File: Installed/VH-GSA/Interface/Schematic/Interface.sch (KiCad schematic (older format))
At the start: 32 parts, among them J1 RJ45, J2 RJ12, J3 RJ12, P1 USB_B, P10 USB_A, P11 USB_A, P12 USB_A, P13 USB_A, P14 USB_A, P15 USB_A, P16 USB_A, P17 USB_A, P2 USB_B, P3 CONN_01X02, P4 USB_B, P5 USB_B, P6 CONN_01X06, P7 CONN_01X06, P8 CONN_01X06, P9 CONN_01X06, SW1 SW_DPDT_x2, U1 MAX232

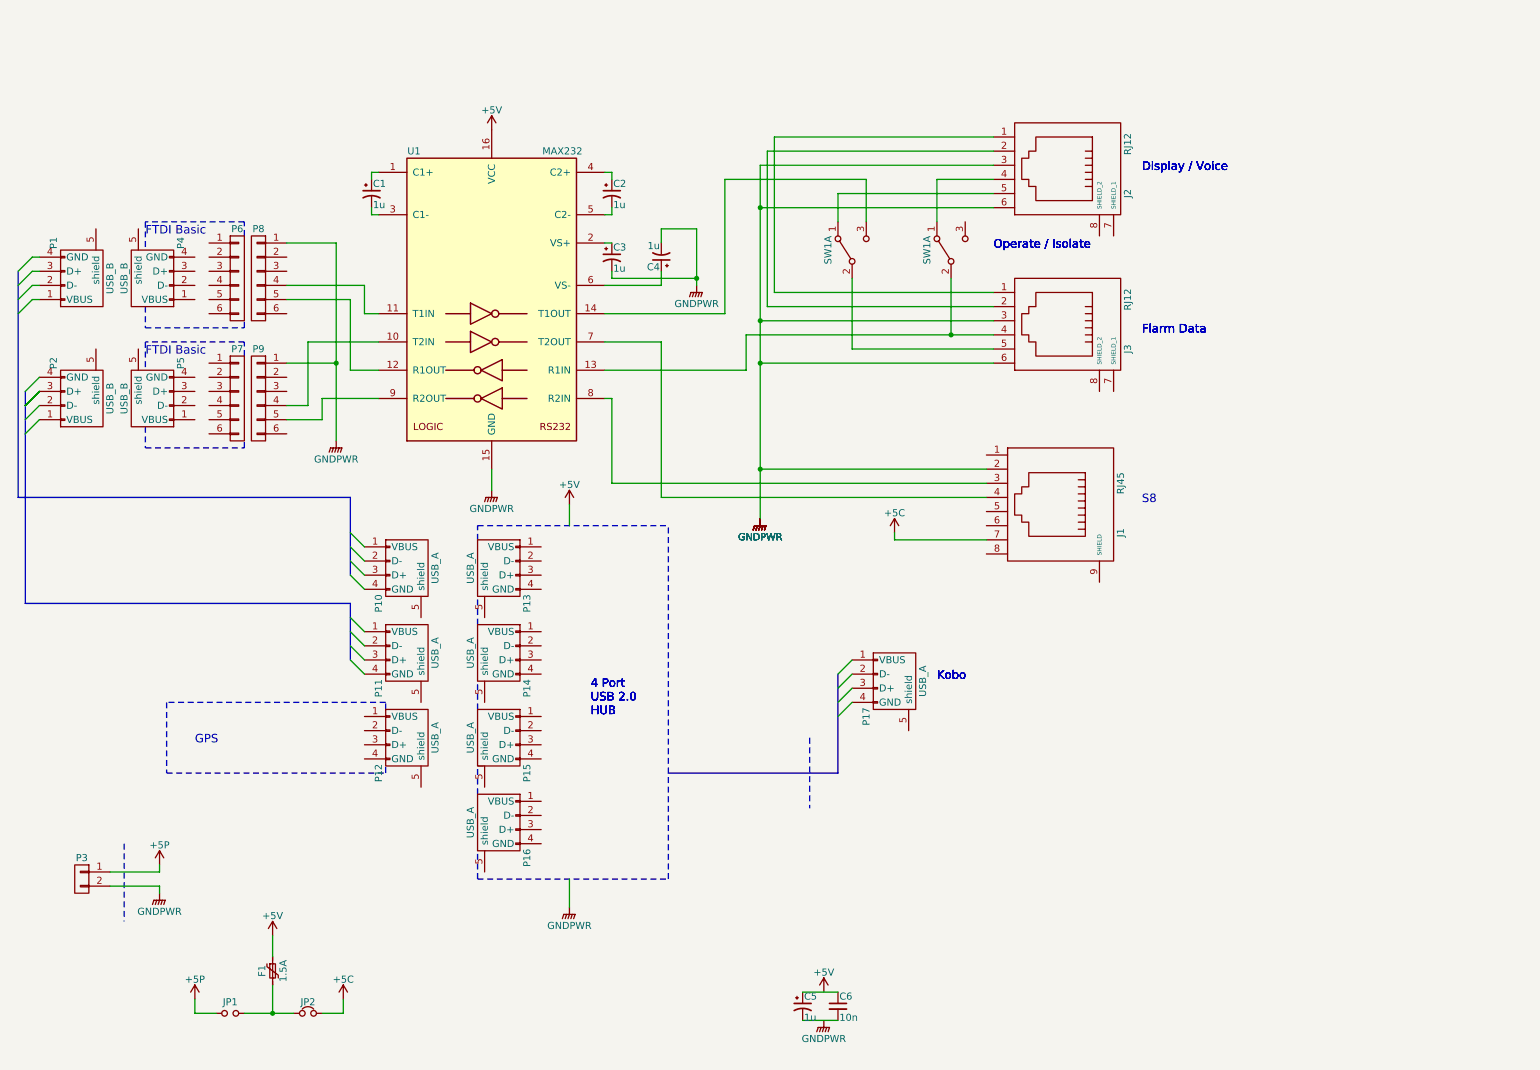
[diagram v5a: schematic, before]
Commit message: VH-GSA: Removed Flarm loop through
This version assumes that the Flatm Redbox is connected to the S8
Vario.
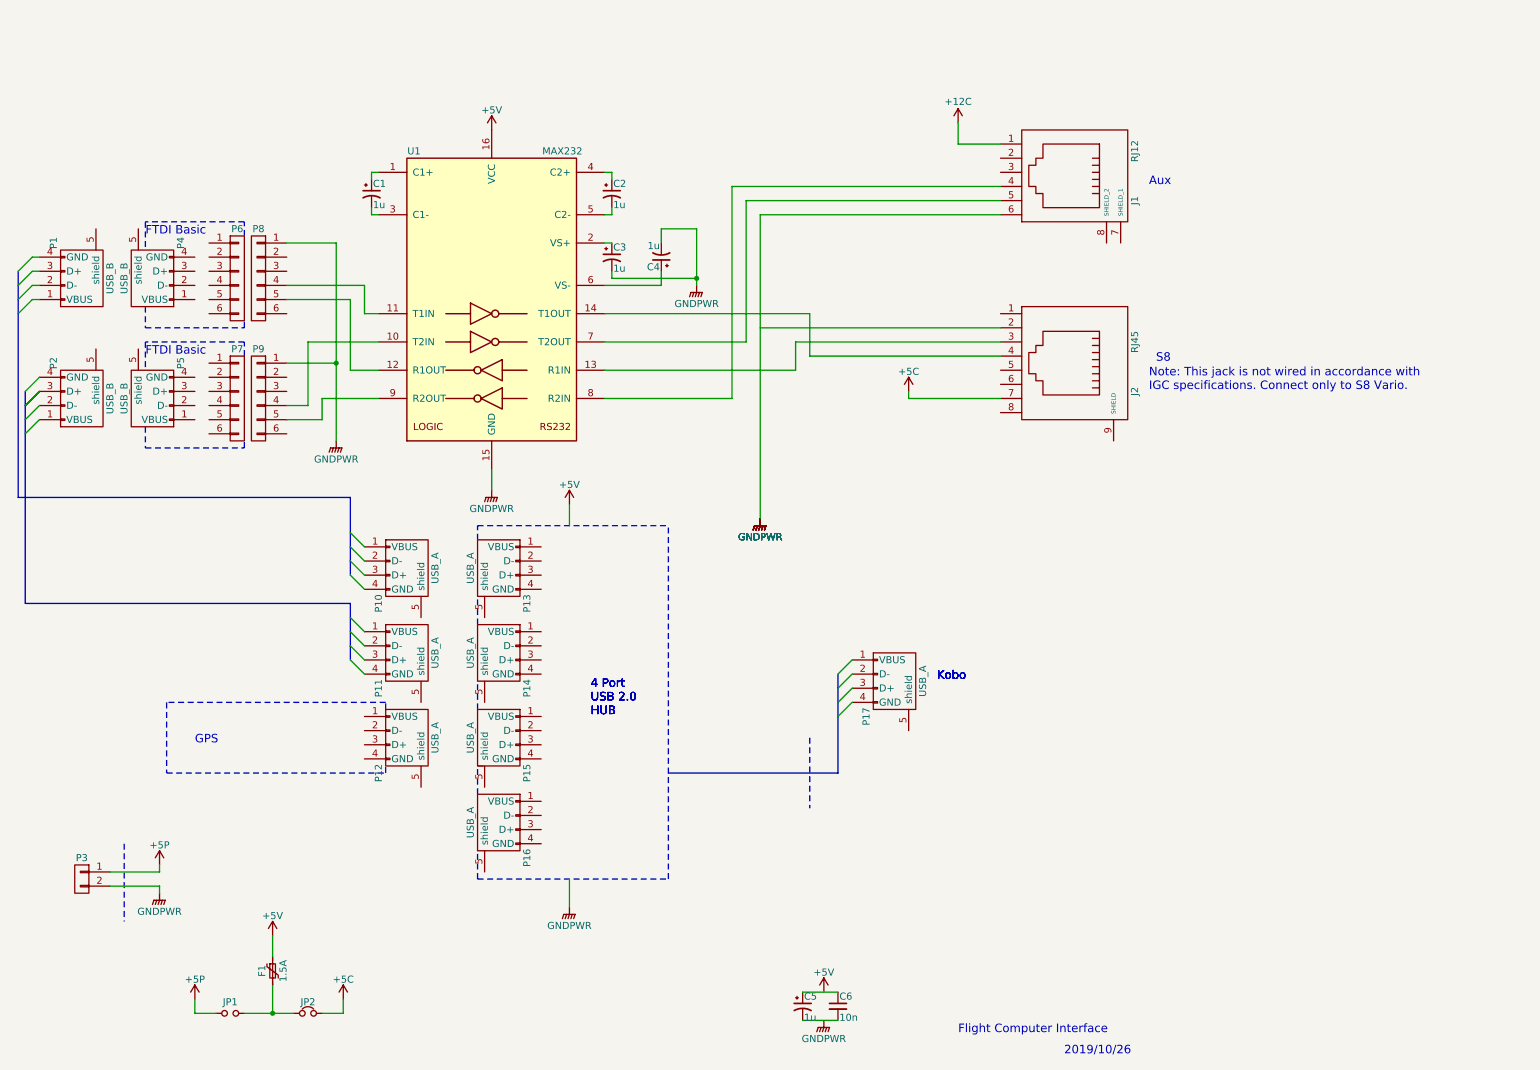
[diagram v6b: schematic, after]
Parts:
- removed J2: RJ12, symbol RJ12
- removed SW1 (x2): SW_DPDT_x2, symbol SW_DPDT_x2
- renumbered J3 to J1, J1 to J2
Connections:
- net labels added: +12C
- wire segments 85 -> 73
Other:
- note added: "2019/10/26"
- note added: "Aux"
- note added: "Flight Computer Interface"
- note added: "Note: This jack is not wired in accordance with\nIGC specifications. Connect only to S8 Vario."
- note removed: "Display / Voice"
- note removed: "Flarm Data"
- note removed: "Operate / Isolate"
- moved on the sheet: J1, J2

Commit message: VH-GSA: Corrected C4 polarity
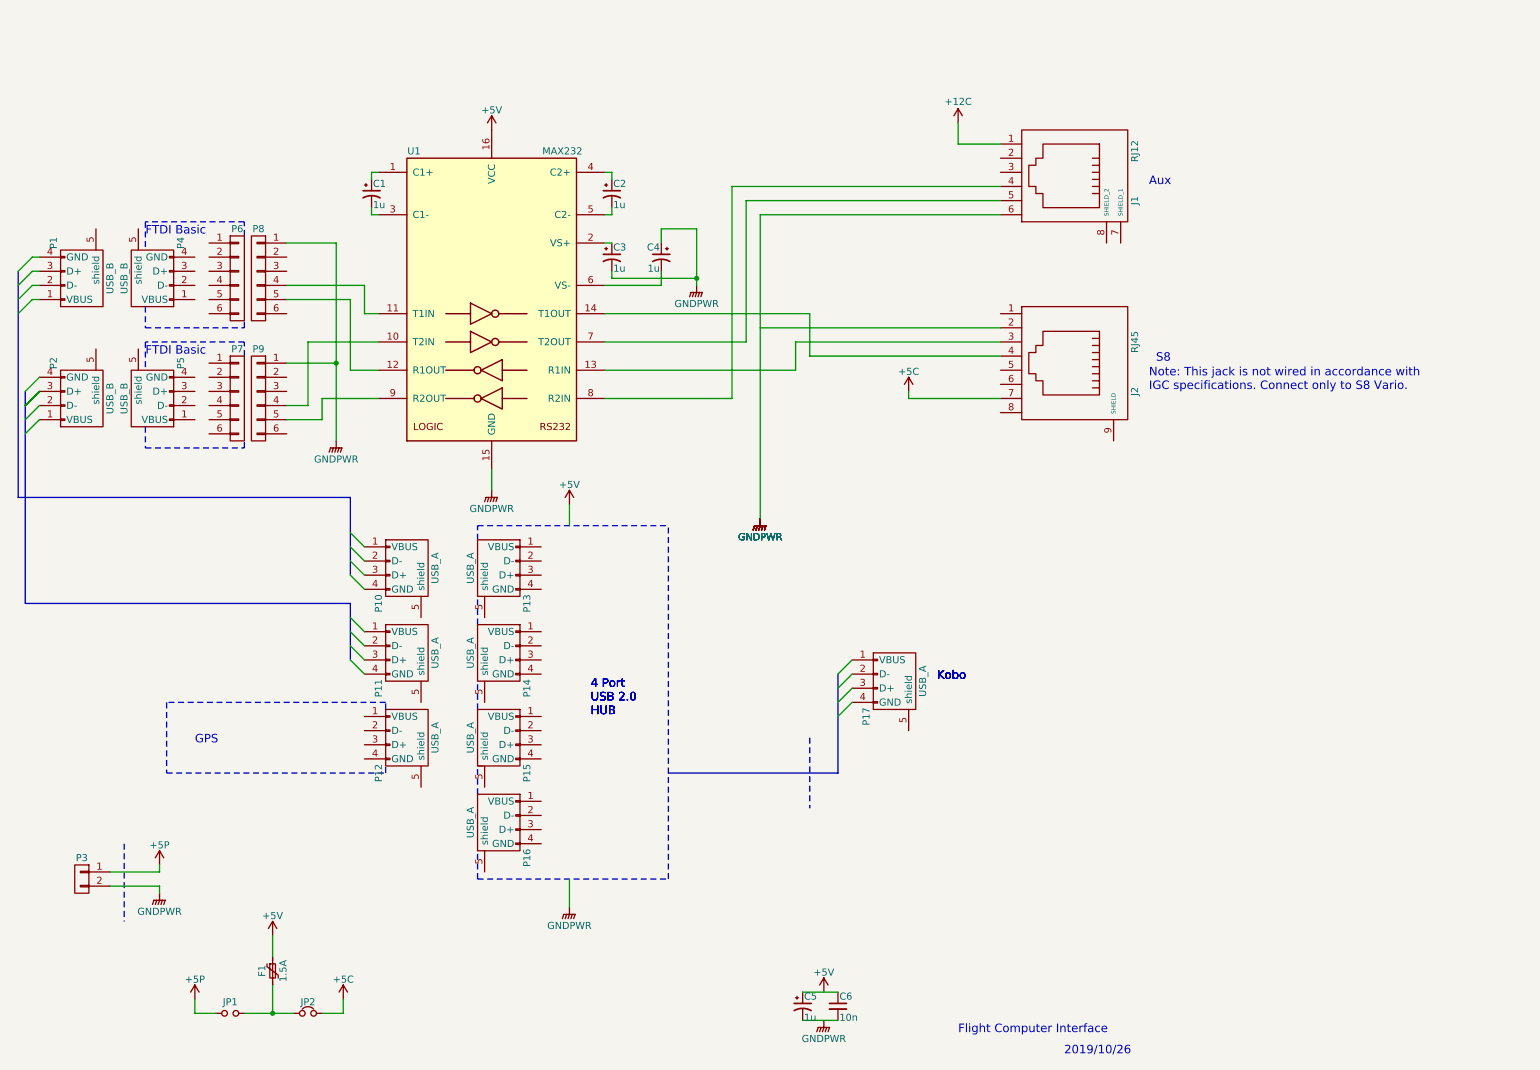
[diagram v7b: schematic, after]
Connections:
- wire segments 73 -> 70
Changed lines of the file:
@@
 F 3 "" H 5300 2000 50  0000 C CNN
 	1    5300 2000
-	-1   0    0    1
+	-1   0    0    -1
 $EndComp
 $Comp
@@
 	5300 1800 5550 1800
 Wire Wire Line
-	5550 1800 5550 2150
-Wire Wire Line
-	5550 2150 5550 2200
+	5550 1800 5550 2200
 Wire Wire Line
 	4950 2150 5550 2150
@@
 	6300 7400 6550 7400
 Wire Bus Line
-	750  2100 750  2200
-Wire Bus Line
-	750  2200 750  2300
-Wire Bus Line
-	750  2300 750  2400
-Wire Bus Line
-	750  2400 750  3700
+	750  2100 750  3700
 Wire Wire Line
 	850  2000 900  2000
@@
 	750  3700 3100 3700
 Wire Bus Line
-	3100 3700 3100 3950
+	3100 3700 3100 4250
 Wire Bus Line
-	3100 3950 3100 4050
-Wire Bus Line
-	3100 4050 3100 4150
-Wire Bus Line
-	3100 4150 3100 4250
-Wire Bus Line
-	800  2950 800  3050
-Wire Bus Line
-	800  3050 800  3150
-Wire Bus Line
-	800  3150 800  3250
-Wire Bus Line
-	800  3250 800  4450
+	800  2950 800  4450
 Wire Bus Line
 	800  4450 3100 4450
 Wire Bus Line
-	3100 4450 3100 4550
-Wire Bus Line
-	3100 4550 3100 4650
-Wire Bus Line
-	3100 4650 3100 4750
-Wire Bus Line
-	3100 4750 3100 4850
+	3100 4450 3100 4850
 Wire Notes Line
 	4000 4000 4000 3900
@@
 	5350 6400 5350 3900
 Wire Bus Line
-	6550 4950 6550 5050
-Wire Bus Line
-	6550 5050 6550 5150
-Wire Bus Line
-	6550 5150 6550 5250
-Wire Bus Line
-	6550 5250 6550 5650
+	6550 4950 6550 5650
 Wire Bus Line
 	6550 5650 5350 5650
@@
 	2000 7350 2150 7350
 Wire Wire Line
-	2350 7350 2550 7350
-Wire Wire Line
-	2550 7350 2700 7350
+	2350 7350 2700 7350
 Wire Wire Line
 	2900 7350 3050 7350
@@
 	2650 1900 3000 1900
 Wire Wire Line
-	3000 1900 3000 2750
-Wire Wire Line
-	3000 2750 3000 3300
+	3000 1900 3000 3300
 Wire Wire Line
 	2650 2750 3000 2750
